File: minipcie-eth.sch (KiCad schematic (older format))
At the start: 7 parts

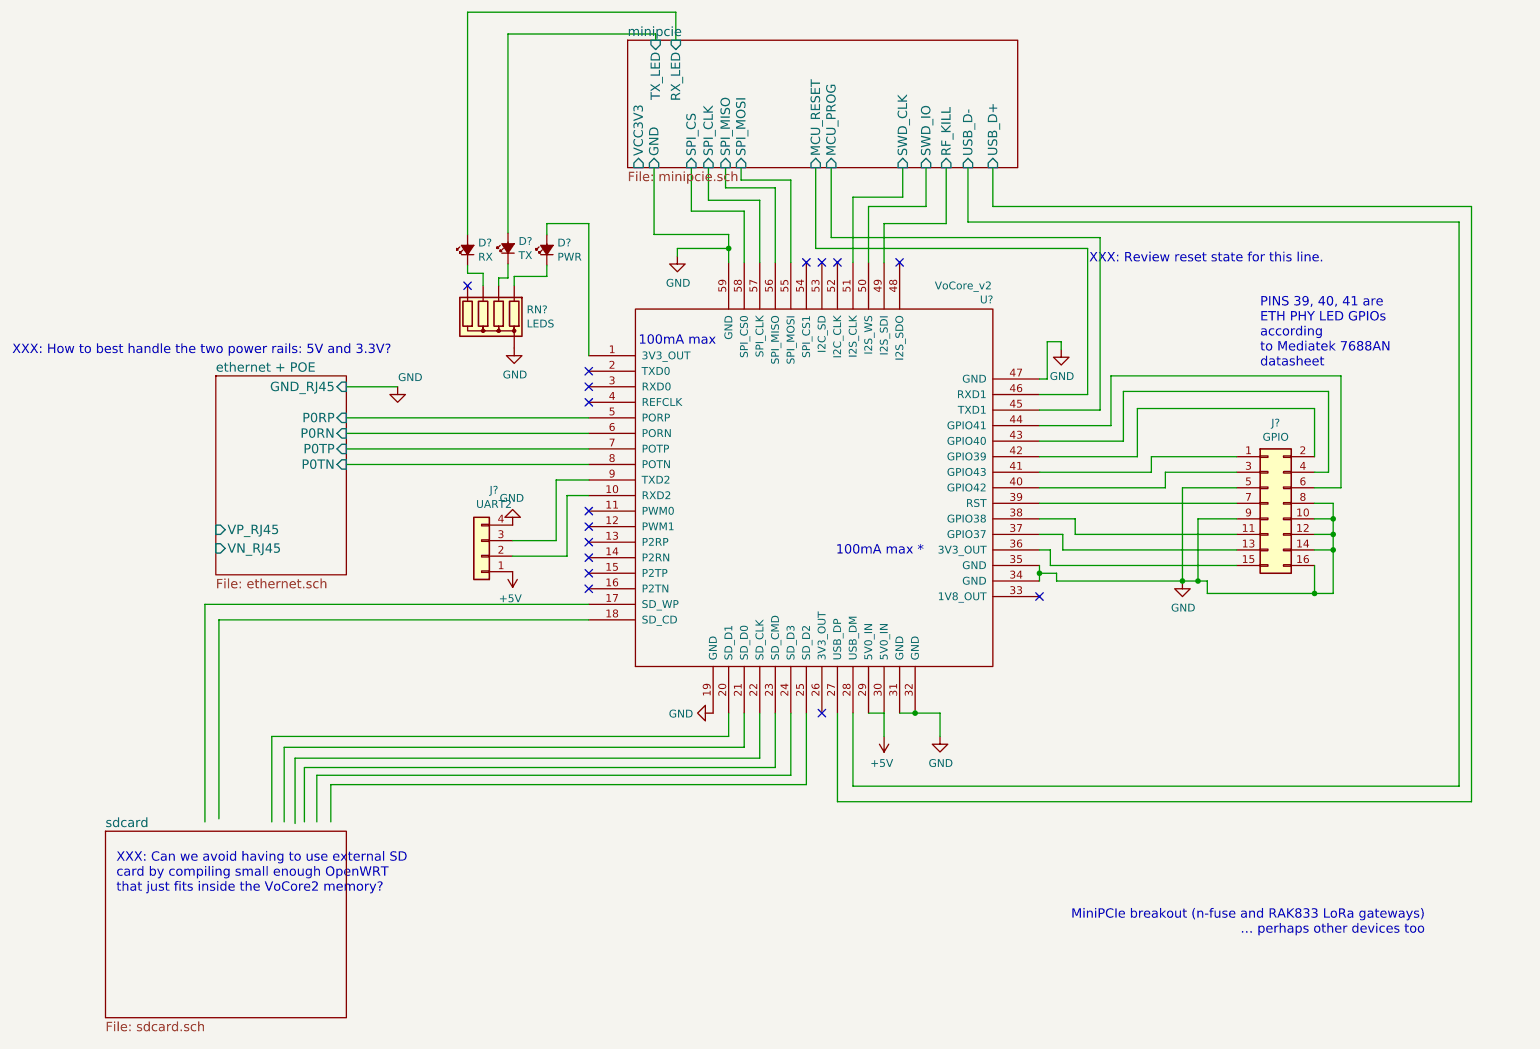
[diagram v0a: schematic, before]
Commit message: Add all POE logic with the si3404, schematic almost finished.
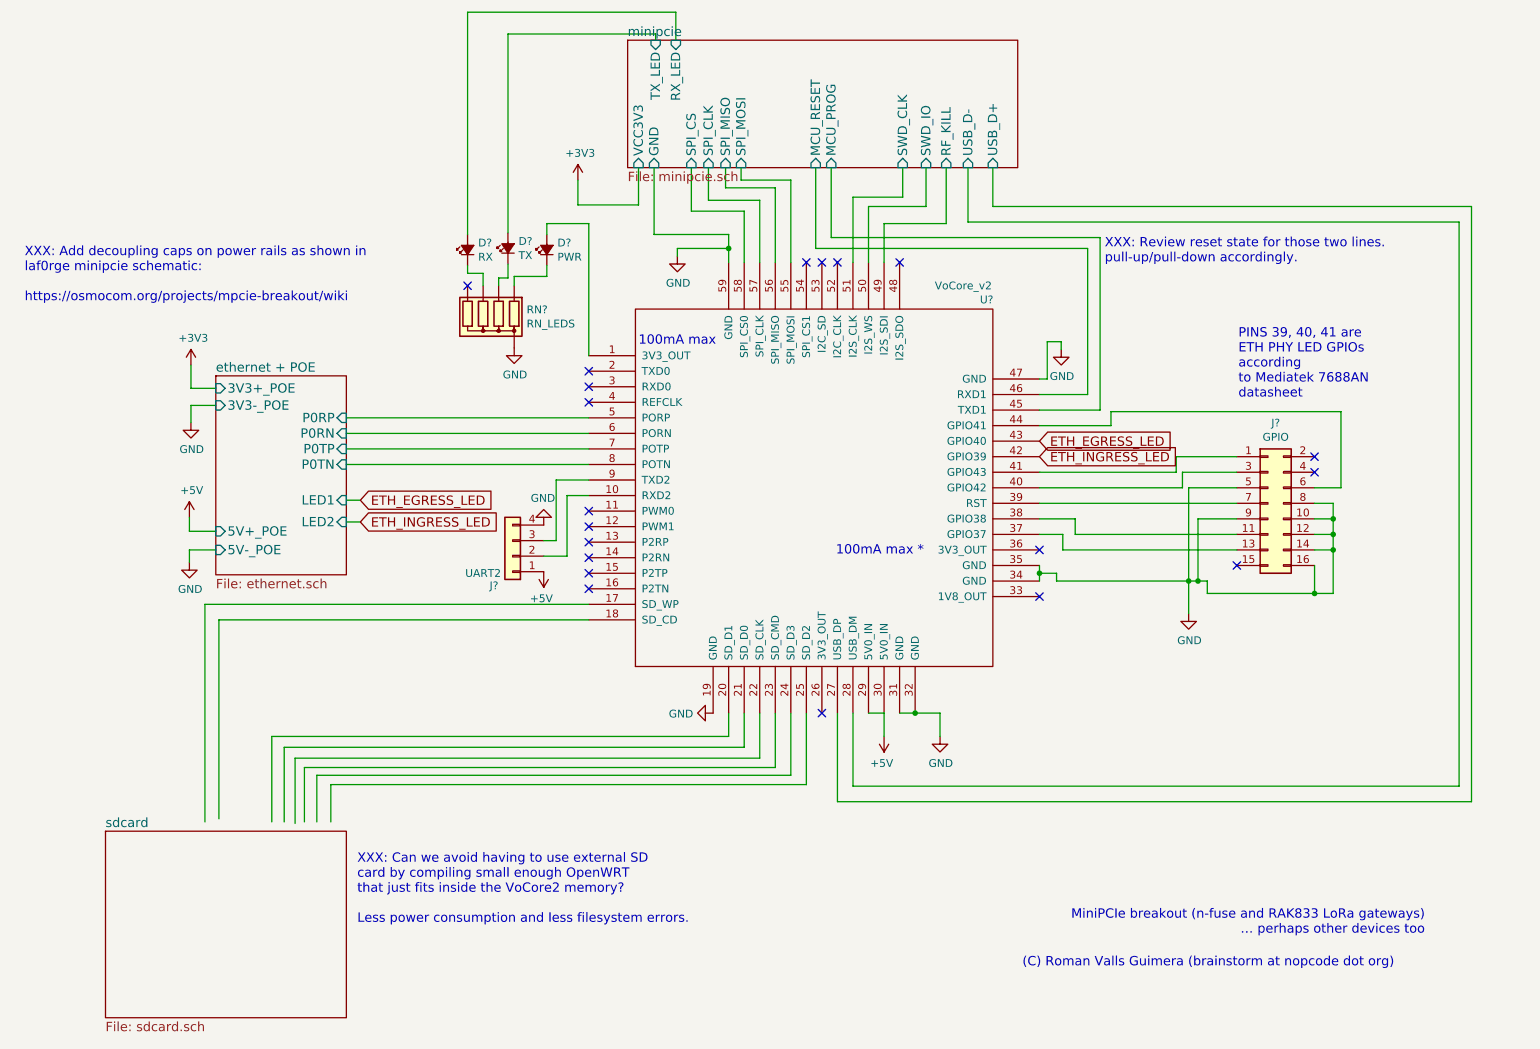
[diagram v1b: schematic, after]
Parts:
- RN?: value LEDS -> RN_LEDS
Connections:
- net labels added: +3V3, ETH_EGRESS_LED, ETH_INGRESS_LED
- wire segments 149 -> 159
- no-connect marks 16 -> 20
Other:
- note added: "(C) Roman Valls Guimera (brainstorm at nopcode dot org)"
- note added: "XXX: Add decoupling caps on power rails as shown in\nlaf0rge minipcie schematic:\n\nhttps://osmocom.org/projects/mpcie-breakout/wiki"
- note added: "XXX: Can we avoid having to use external SD \ncard by compiling small enough OpenWRT \nthat just fits inside the VoCore2 memory?\n\nLess power consumption and less filesystem errors."
- note added: "XXX: Review reset state for those two lines.\npull-up/pull-down accordingly."
- note removed: "XXX: Can we avoid having to use external SD \ncard by compiling small enough OpenWRT \nthat just fits inside the VoCore2 memory?"
- note removed: "XXX: How to best handle the two power rails: 5V and 3.3V?"
- note removed: "XXX: Review reset state for this line."
- moved on the sheet: J?
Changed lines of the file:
@@
 LIBS:mpcie
 LIBS:si3406
+LIBS:si3404
+LIBS:SI-52003-F
+LIBS:ap2112
 LIBS:minipcie-eth-cache
 EELAYER 26 0
@@
 F4 "P0TP" I R 2700 3680 60
 F5 "P0TN" I R 2700 3780 60
-F6 "VP_RJ45" I L 1860 4200 60
-F7 "VN_RJ45" I L 1860 4320 60
-F8 "GND_RJ45" I R 2700 3280 60
+F6 "5V+_POE" I L 1860 4210 60
+F7 "5V-_POE" I L 1860 4330 60
+F8 "LED1" I R 2700 4010 60
+F9 "LED2" I R 2700 4150 60
+F10 "3V3+_POE" I L 1860 3290 60
+F11 "3V3-_POE" I L 1860 3400 60
 $EndSheet
 $Sheet
@@
 L Conn_01x04 J?
 U 1 1 5BAF1493
-P 3570 4370
-F 0 "J?" H 3490 3945 50  0000 C CNN
-F 1 "UART2" H 3490 4036 50  0000 C CNN
-F 2 "" H 3570 4370 50  0001 C CNN
-F 3 "" H 3570 4370 50  0001 C CNN
-	1    3570 4370
+P 3770 4370
+F 0 "J?" H 3890 4560 50  0000 C CNN
+F 1 "UART2" H 3960 4480 50  0000 C CNN
+F 2 "" H 3770 4370 50  0001 C CNN
+F 3 "" H 3770 4370 50  0001 C CNN
+	1    3770 4370
 	-1   0    0    1
 $EndComp
@@
 L GND #PWR?
 U 1 1 5BAF158B
-P 8080 4530
-F 0 "#PWR?" H 8080 4280 50  0001 C CNN
-F 1 "GND" H 8085 4357 50  0000 C CNN
-F 2 "" H 8080 4530 50  0001 C CNN
-F 3 "" H 8080 4530 50  0001 C CNN
-	1    8080 4530
+P 8120 4740
+F 0 "#PWR?" H 8120 4490 50  0001 C CNN
+F 1 "GND" H 8125 4567 50  0000 C CNN
+F 2 "" H 8120 4740 50  0001 C CNN
+F 3 "" H 8120 4740 50  0001 C CNN
+	1    8120 4740
 	1    0    0    -1
 $EndComp
@@
 L +5V #PWR?
 U 1 1 5BAF2AC1
-P 3770 4470
-F 0 "#PWR?" H 3770 4320 50  0001 C CNN
-F 1 "+5V" H 3785 4643 50  0000 C CNN
-F 2 "" H 3770 4470 50  0001 C CNN
-F 3 "" H 3770 4470 50  0001 C CNN
-	1    3770 4470
+P 3970 4470
+F 0 "#PWR?" H 3970 4320 50  0001 C CNN
+F 1 "+5V" H 3985 4643 50  0000 C CNN
+F 2 "" H 3970 4470 50  0001 C CNN
+F 3 "" H 3970 4470 50  0001 C CNN
+	1    3970 4470
 	-1   0    0    1
 $EndComp
@@
 L GND #PWR?
 U 1 1 5BAF2AD4
-P 3770 4170
-F 0 "#PWR?" H 3770 3920 50  0001 C CNN
-F 1 "GND" H 3775 3997 50  0000 C CNN
-F 2 "" H 3770 4170 50  0001 C CNN
-F 3 "" H 3770 4170 50  0001 C CNN
-	1    3770 4170
+P 3970 4170
+F 0 "#PWR?" H 3970 3920 50  0001 C CNN
+F 1 "GND" H 3975 3997 50  0000 C CNN
+F 2 "" H 3970 4170 50  0001 C CNN
+F 3 "" H 3970 4170 50  0001 C CNN
+	1    3970 4170
 	-1   0    0    1
 $EndComp
@@
 NoConn ~ 4260 3380
 NoConn ~ 5760 5380
-Text Notes 8580 3160 0    60   ~ 0
+Text Notes 8440 3360 0    60   ~ 0
 PINS 39, 40, 41 are \nETH PHY LED GPIOs \naccording\nto Mediatek 7688AN\ndatasheet
 Text Notes 4580 3020 0    60   ~ 0
@@
 	6160 5380 6160 5530
 Wire Wire Line
-	6260 5380 6520 5380
+	6260 5380 6360 5380
+Wire Wire Line
+	6360 5380 6520 5380
 Wire Wire Line
 	6520 5380 6520 5530
 Connection ~ 6360 5380
 Wire Wire Line
-	5160 2300 5160 2480
+	5160 2300 5160 2390
+Wire Wire Line
+	5160 2390 5160 2480
 Wire Wire Line
 	5160 2390 4830 2390
@@
 	4830 2390 4830 2440
 Wire Wire Line
-	7160 4430 7160 4530
-Wire Wire Line
-	7270 4530 8240 4530
+	7160 4430 7160 4480
+Wire Wire Line
+	7160 4480 7160 4530
+Wire Wire Line
+	7270 4530 8120 4530
+Wire Wire Line
+	8120 4530 8180 4530
+Wire Wire Line
+	8180 4530 8240 4530
 Wire Wire Line
 	8240 4530 8240 4610
 Wire Wire Line
-	8240 4610 9050 4610
+	8240 4610 8930 4610
+Wire Wire Line
+	8930 4610 9050 4610
 Wire Wire Line
 	8930 4610 8930 4430
 Wire Wire Line
-	8430 4430 7230 4430
-Wire Wire Line
-	7230 4430 7230 4330
-Wire Wire Line
-	7230 4330 7160 4330
-Wire Wire Line
 	7160 4230 7310 4230
 Wire Wire Line
@@
 	7160 4030 8430 4030
 Wire Wire Line
-	8430 3930 8080 3930
-Wire Wire Line
-	8080 3930 8080 4530
-Connection ~ 8080 4530
+	8430 3930 8120 3930
+Wire Wire Line
+	8120 3930 8120 4530
+Wire Wire Line
+	8120 4530 8120 4740
+Connection ~ 8120 4530
 Wire Wire Line
 	8430 4130 8180 4130
@@
 Connection ~ 8180 4530
 Wire Wire Line
-	8430 3830 7970 3830
-Wire Wire Line
-	7970 3830 7970 3930
-Wire Wire Line
-	7970 3930 7160 3930
-Wire Wire Line
-	8430 3730 7880 3730
-Wire Wire Line
-	7880 3730 7880 3830
-Wire Wire Line
-	7880 3830 7160 3830
+	8430 3830 8080 3830
+Wire Wire Line
+	8080 3830 8080 3930
+Wire Wire Line
+	8080 3930 7160 3930
+Wire Wire Line
+	8430 3730 8040 3730
+Wire Wire Line
+	8040 3730 8040 3830
+Wire Wire Line
+	8040 3830 7160 3830
 Wire Wire Line
 	8930 4330 9050 4330
 Wire Wire Line
-	9050 4610 9050 4030
+	9050 4610 9050 4330
+Wire Wire Line
+	9050 4330 9050 4230
+Wire Wire Line
+	9050 4230 9050 4130
+Wire Wire Line
+	9050 4130 9050 4030
 Connection ~ 8930 4610
 Wire Wire Line
-	7160 3730 7790 3730
-Wire Wire Line
-	7790 3730 7790 3420
-Wire Wire Line
-	7790 3420 8930 3420
-Wire Wire Line
-	8930 3420 8930 3730
-Wire Wire Line
-	7160 3630 7700 3630
-Wire Wire Line
-	7700 3630 7700 3310
-Wire Wire Line
-	7700 3310 9020 3310
-Wire Wire Line
-	9020 3310 9020 3830
-Wire Wire Line
-	9020 3830 8930 3830
-Wire Wire Line
 	7160 3530 7620 3530
 Wire Wire Line
-	7620 3530 7620 3210
-Wire Wire Line
-	7620 3210 9100 3210
-Wire Wire Line
-	9100 3210 9100 3930
+	7620 3530 7620 3440
+Wire Wire Line
+	7620 3440 9100 3440
+Wire Wire Line
+	9100 3440 9100 3930
 Wire Wire Line
 	9100 3930 8930 3930
@@
 	4120 3980 4120 4370
 Wire Wire Line
-	4120 4370 3770 4370
+	4120 4370 3970 4370
 Wire Wire Line
 	4260 3880 4050 3880
@@
 	4050 3880 4050 4270
 Wire Wire Line
-	4050 4270 3770 4270
+	4050 4270 3970 4270
 Wire Wire Line
 	5860 5380 5860 5950
@@
 Wire Wire Line
 	6560 2230 6560 1870
-Text Notes 1220 6540 0    60   ~ 0
-XXX: Can we avoid having to use external SD \ncard by compiling small enough OpenWRT \nthat just fits inside the VoCore2 memory?
-Text Notes 7480 2490 0    60   ~ 0
-XXX: Review reset state for this line.
-Text Notes 550  3080 0    60   ~ 0
-XXX: How to best handle the two power rails: 5V and 3.3V?
+Text Notes 2770 6740 0    60   ~ 0
+XXX: Can we avoid having to use external SD \ncard by compiling small enough OpenWRT \nthat just fits inside the VoCore2 memory?\n\nLess power consumption and less filesystem errors.
+Text Notes 7580 2490 0    60   ~ 0
+XXX: Review reset state for those two lines.\npull-up/pull-down accordingly.
 $Comp
 L LED_Small_ALT D?
@@
 P 3580 2830
 F 0 "RN?" H 3300 2784 50  0000 R CNN
-F 1 "LEDS" H 3300 2875 50  0000 R CNN
+F 1 "RN_LEDS" H 3300 2875 50  0000 R CNN
 F 2 "Resistors_THT:R_Array_SIP5" V 3855 2830 50  0001 C CNN
 F 3 "" H 3580 2830 50  0001 C CNN
@@
 	3580 2550 3580 2630
 NoConn ~ 3480 2630
-$Comp
-L GND #PWR?
-U 1 1 5BC0BA99
-P 3030 3280
-F 0 "#PWR?" H 3030 3030 50  0001 C CNN
-F 1 "GND" H 3190 3340 50  0000 R CNN
-F 2 "" H 3030 3280 50  0001 C CNN
-F 3 "" H 3030 3280 50  0001 C CNN
-	1    3030 3280
-	1    0    0    -1
-$EndComp
-Wire Wire Line
-	3030 3280 2700 3280
 Wire Wire Line
 	7270 4530 7270 4480
@@
 Wire Wire Line
 	7300 2990 7300 3040
+Text Notes 7050 7020 0    60   ~ 0
+(C) Roman Valls Guimera (brainstorm at nopcode dot org)
+$Comp
+L GND #PWR?
+U 1 1 5BC3827A
+P 1690 4410
+F 0 "#PWR?" H 1690 4160 50  0001 C CNN
+F 1 "GND" H 1695 4237 50  0000 C CNN
+F 2 "" H 1690 4410 50  0001 C CNN
+F 3 "" H 1690 4410 50  0001 C CNN
+	1    1690 4410
+	1    0    0    -1
+$EndComp
+Wire Wire Line
+	1860 4330 1690 4330
+Wire Wire Line
+	1690 4330 1690 4410
+Wire Wire Line
+	1860 4210 1690 4210
+Wire Wire Line
+	1690 4210 1690 4120
+$Comp
+L +5V #PWR?
+U 1 1 5BC389B7
+P 1690 4120
+F 0 "#PWR?" H 1690 3970 50  0001 C CNN
+F 1 "+5V" H 1705 4293 50  0000 C CNN
+F 2 "" H 1690 4120 50  0001 C CNN
+F 3 "" H 1690 4120 50  0001 C CNN
+	1    1690 4120
+	1    0    0    -1
+$EndComp
+$Comp
+L GND #PWR?
+U 1 1 5BC444DB
+P 1700 3510
+F 0 "#PWR?" H 1700 3260 50  0001 C CNN
+F 1 "GND" H 1705 3337 50  0000 C CNN
+F 2 "" H 1700 3510 50  0001 C CNN
+F 3 "" H 1700 3510 50  0001 C CNN
+	1    1700 3510
+	1    0    0    -1
+$EndComp
+Wire Wire Line
+	1860 3400 1700 3400
+Wire Wire Line
+	1700 3400 1700 3510
+Wire Wire Line
+	1860 3290 1700 3290
+Wire Wire Line
+	1700 3290 1700 3140
+Text GLabel 2790 4010 2    60   Input ~ 0
+ETH_EGRESS_LED
+Text GLabel 2790 4150 2    60   Input ~ 0
+ETH_INGRESS_LED
+Wire Wire Line
+	2790 4010 2700 4010
+Wire Wire Line
+	2700 4150 2790 4150
+Text GLabel 7160 3630 2    60   Input ~ 0
+ETH_EGRESS_LED
+Text GLabel 7160 3730 2    60   Input ~ 0
+ETH_INGRESS_LED
+$Comp
+L +3V3 #PWR?
+U 1 1 5BC46C2B
+P 1700 3140
+F 0 "#PWR?" H 1700 2990 50  0001 C CNN
+F 1 "+3V3" H 1715 3313 50  0000 C CNN
+F 2 "" H 1700 3140 50  0001 C CNN
+F 3 "" H 1700 3140 50  0001 C CNN
+	1    1700 3140
+	1    0    0    -1
+$EndComp
+$Comp
+L +3V3 #PWR?
+U 1 1 5BC46E95
+P 4190 1950
+F 0 "#PWR?" H 4190 1800 50  0001 C CNN
+F 1 "+3V3" H 4205 2123 50  0000 C CNN
+F 2 "" H 4190 1950 50  0001 C CNN
+F 3 "" H 4190 1950 50  0001 C CNN
+	1    4190 1950
+	1    0    0    -1
+$EndComp
+Wire Wire Line
+	4580 1870 4580 2110
+Wire Wire Line
+	4580 2110 4190 2110
+Wire Wire Line
+	4190 2110 4190 1950
+NoConn ~ 8930 3830
+NoConn ~ 8930 3730
+NoConn ~ 7160 4330
+NoConn ~ 8430 4430
+Text Notes 630  2740 0    60   ~ 0
+XXX: Add decoupling caps on power rails as shown in\nlaf0rge minipcie schematic:\n\nhttps://osmocom.org/projects/mpcie-breakout/wiki
 $EndSCHEMATC
